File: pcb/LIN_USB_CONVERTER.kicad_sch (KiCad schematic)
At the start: 32 parts, among them J1 Conn_01x03, J2 TerminalBlock, J4 USB_C_Receptacle_USB2.0_16P, J6 Conn_ARM_SWD_TagConnect_TC203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, U1 TJA1028T/3V3/20/1J, U2 ISO7321CDR, U3 MCP1700T-3302ETT, U4 STM32F042G6U6

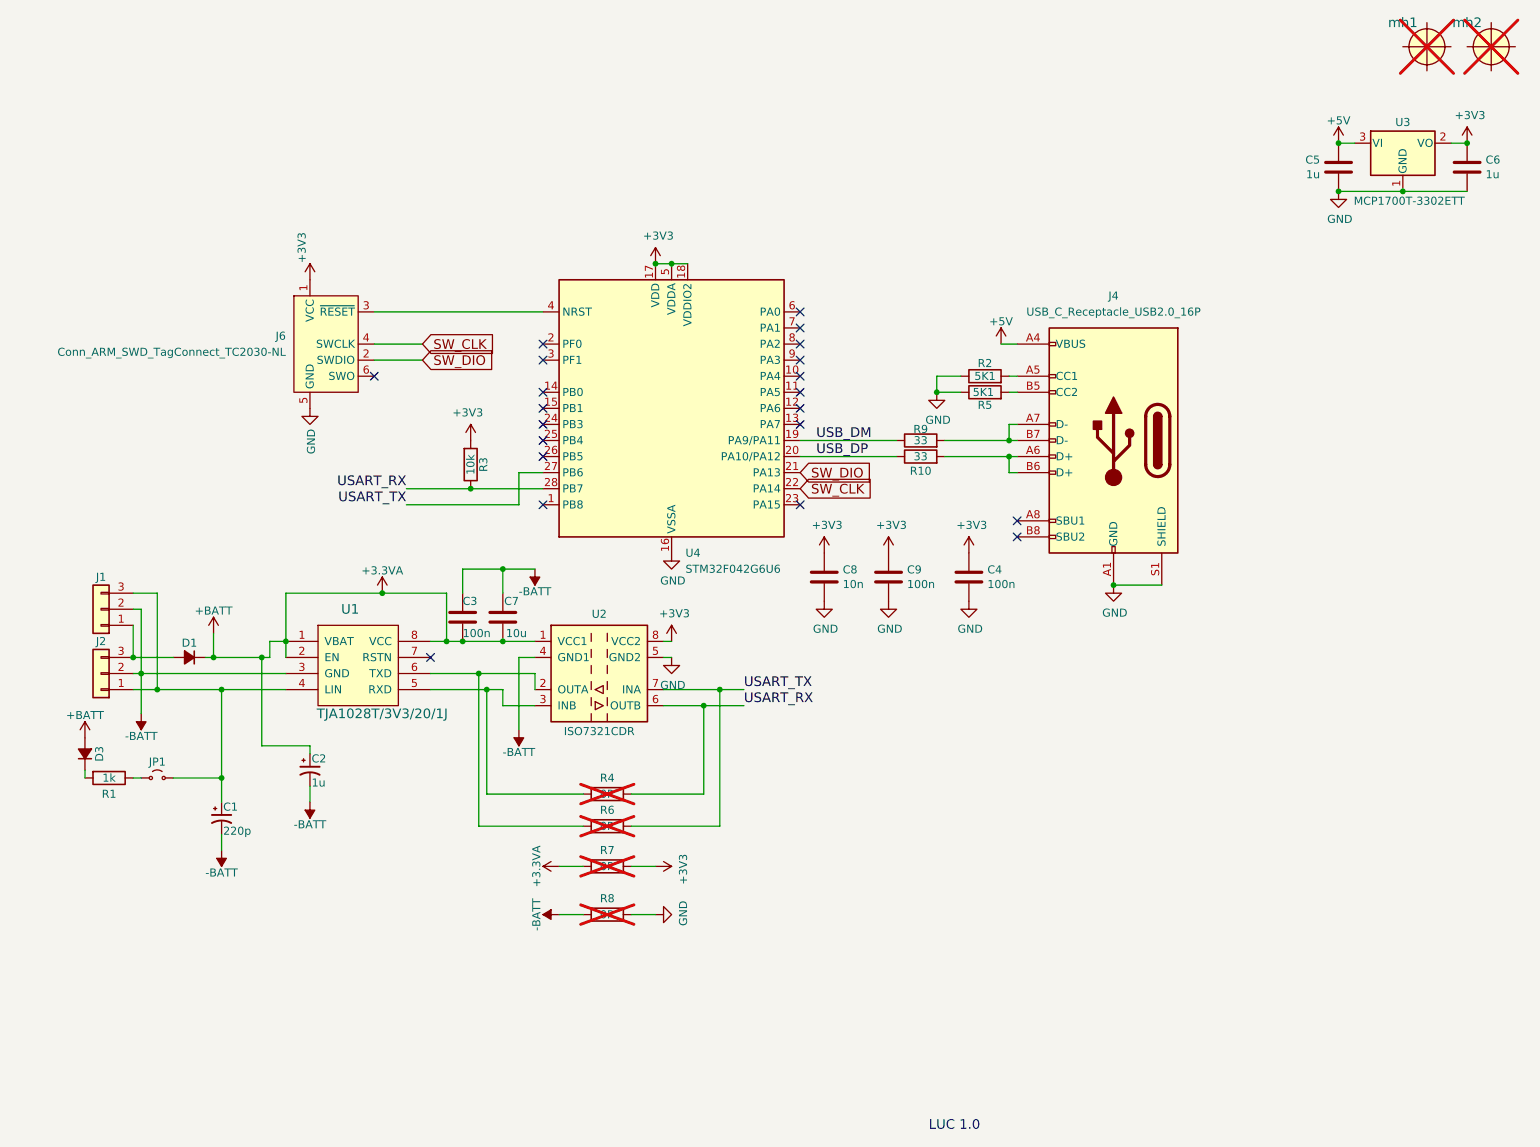
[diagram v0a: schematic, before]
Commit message: moved terminals to top, added mounting holes
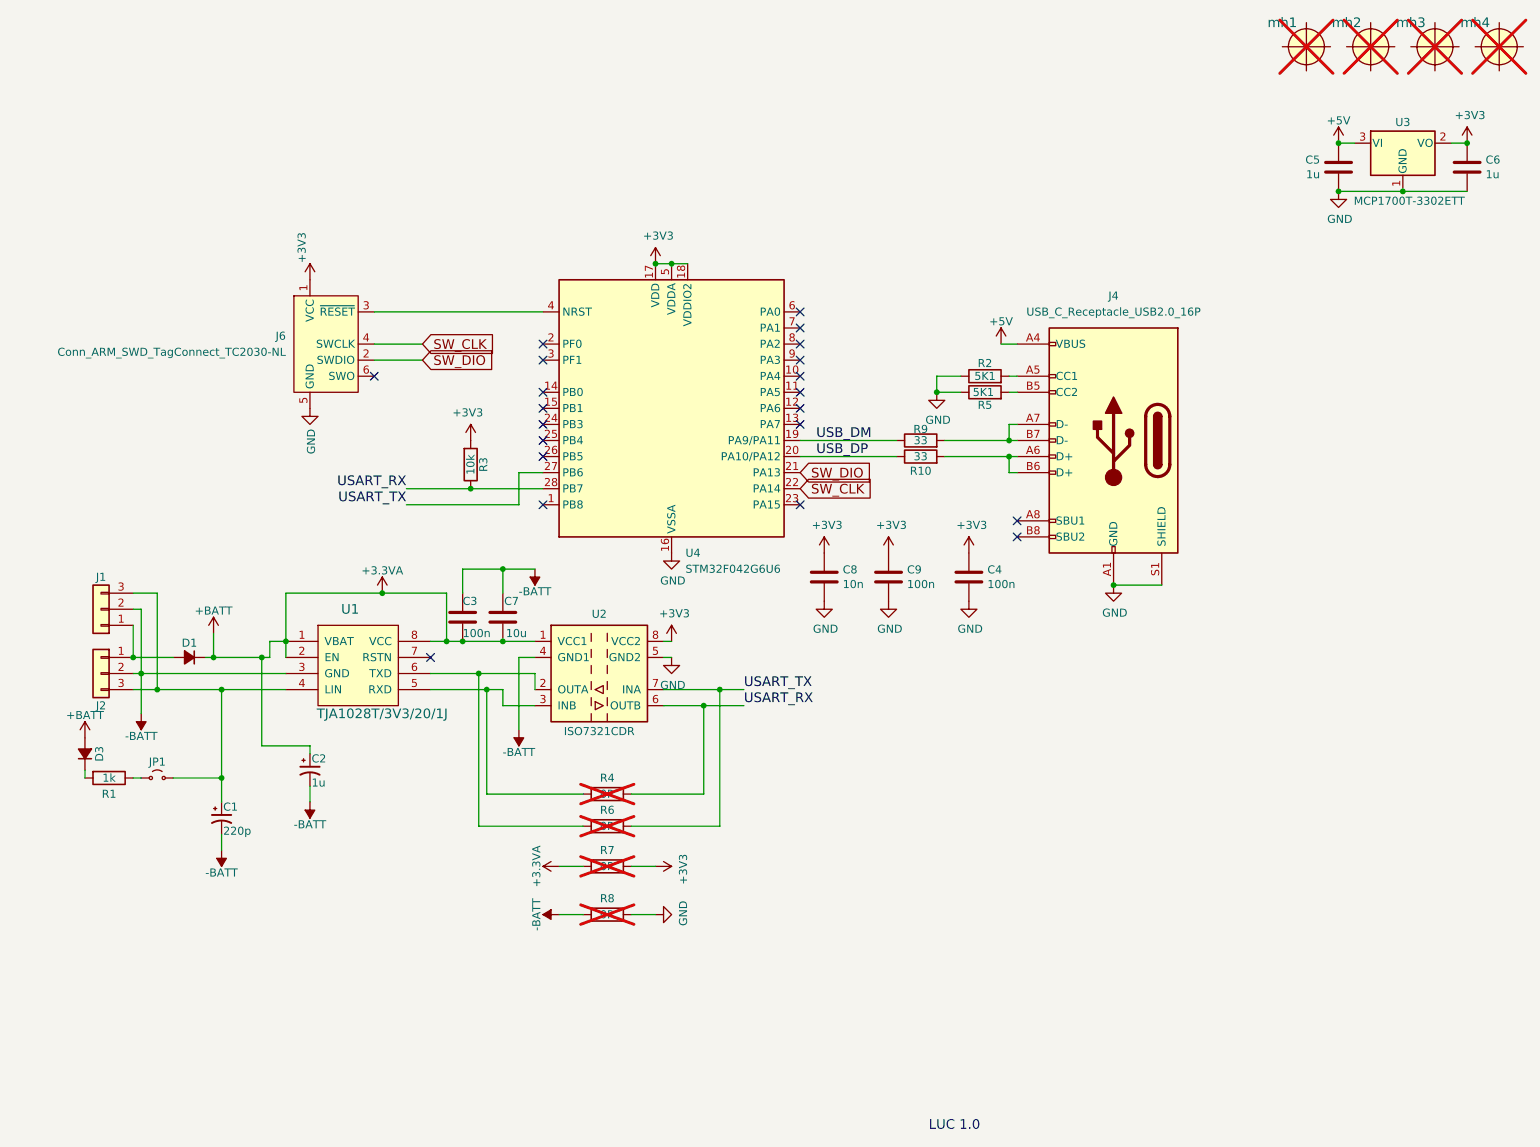
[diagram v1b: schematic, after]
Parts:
- added mh3, mh4: fiducial, usb_ccb_custom:1pin, symbol LIN_USB_CONVERTER-rescue:fiducial-RESCUE-LIN_USB_CONVERTER
- J1: LCSC Part # (none) -> C49257
- J2: footprint TerminalBlock:TerminalBlock_Altech_AK300-3_P5.00mm -> TerminalBlock_Phoenix:TerminalBlock_Phoenix_MKDS-1,5-3_1x03_P5.00mm_Horizontal; LCSC Part # (none) -> C424695; LSCS Part # C5188437 -> (none)
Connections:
- net at C1.1, J1.3 (Pin_3), JP1.2 (B)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: now also J2.3 (Pin_3); no longer J2.1 (Pin_1)
- net at D1.1 (A), J1.1 (Pin_1): now also J2.1 (Pin_1); no longer J2.3 (Pin_3)
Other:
- moved on the sheet: J2, mh1, mh2
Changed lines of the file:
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@@
 	(symbol
 		(lib_id "LIN_USB_CONVERTER-rescue:fiducial-RESCUE-LIN_USB_CONVERTER")
-		(at 266.7 19.05 0)
+		(at 247.65 19.05 0)
 		(unit 1)
 		(exclude_from_sim no)
@@
 		(dnp yes)
 		(property "Reference" "mh1"
-			(at 262.89 15.24 0)
+			(at 243.84 15.24 0)
 			(effects
 				(font
@@
 		)
 		(property "Value" "fiducial"
-			(at 273.05 25.4 0)
+			(at 254 25.4 0)
 			(effects
 				(font
@@
 		)
 		(property "Footprint" "usb_ccb_custom:1pin"
-			(at 266.7 19.05 0)
+			(at 247.65 19.05 0)
 			(effects
 				(font
@@
 		)
 		(property "Datasheet" ""
-			(at 266.7 19.05 0)
+			(at 247.65 19.05 0)
 			(effects
 				(font
@@
 		)
 		(property "Description" ""
-			(at 266.7 19.05 0)
+			(at 247.65 19.05 0)
 			(effects
 				(font
@@
 	(symbol
 		(lib_id "LIN_USB_CONVERTER-rescue:Conn_01x03-RESCUE-LIN_USB_CONVERTER")
-		(at 57.15 118.11 180)
+		(at 57.15 118.11 0)
+		(mirror y)
 		(unit 1)
 		(exclude_from_sim no)
@@
 		(dnp no)
 		(property "Reference" "J2"
-			(at 57.15 113.03 0)
+			(at 57.15 123.19 0)
 			(effects
 				(font
@@
 		)
 		(property "Value" "TerminalBlock"
-			(at 57.15 113.03 0)
+			(at 57.15 123.19 0)
 			(effects
 				(font
@@
 			)
 		)
-		(property "Footprint" "TerminalBlock:TerminalBlock_Altech_AK300-3_P5.00mm"
+		(property "Footprint" "TerminalBlock_Phoenix:TerminalBlock_Phoenix_MKDS-1,5-3_1x03_P5.00mm_Horizontal"
 			(at 57.15 118.11 0)
 			(effects
@@
 			)
 		)
-		(property "LSCS Part #" "C5188437"
+		(property "LCSC Part #" "C424695"
 			(at 57.15 118.11 0)
 			(effects
@@
 			)
 		)
+		(property "LCSC Part #" "C49257"
+			(at 57.15 107.95 0)
+			(effects
+				(font
+					(size 1.27 1.27)
+				)
+				(hide yes)
+			)
+		)
 		(pin "2"
 		)
@@
 	(symbol
 		(lib_id "LIN_USB_CONVERTER-rescue:fiducial-RESCUE-LIN_USB_CONVERTER")
-		(at 276.86 19.05 0)
+		(at 257.81 19.05 0)
 		(unit 1)
 		(exclude_from_sim no)
@@
 		(dnp yes)
 		(property "Reference" "mh2"
-			(at 273.05 15.24 0)
+			(at 254 15.24 0)
 			(effects
 				(font
@@
 		)
 		(property "Value" "fiducial"
-			(at 283.21 25.4 0)
+			(at 264.16 25.4 0)
 			(effects
 				(font
@@
 		)
 		(property "Footprint" "usb_ccb_custom:1pin"
-			(at 276.86 19.05 0)
+			(at 257.81 19.05 0)
 			(effects
 				(font
@@
 		)
 		(property "Datasheet" ""
-			(at 276.86 19.05 0)
+			(at 257.81 19.05 0)
 			(effects
 				(font
@@
 		)
 		(property "Description" ""
-			(at 276.86 19.05 0)
+			(at 257.81 19.05 0)
 			(effects
 				(font
@@
 					(unit 1)
 				)
+			)
+		)
+	)
+	(symbol
+		(lib_id "LIN_USB_CONVERTER-rescue:fiducial-RESCUE-LIN_USB_CONVERTER")
+		(at 267.97 19.05 0)
+		(unit 1)
+		(exclude_from_sim no)
+		(in_bom no)
+		(on_board yes)
+		(dnp yes)
+		(property "Reference" "mh3"
+			(at 264.16 15.24 0)
+			(effects
+				(font
+					(size 1.524 1.524)
+				)
+			)
+		)
+		(property "Value" "fiducial"
+			(at 274.32 25.4 0)
+			(effects
+				(font
+					(size 1.524 1.524)
+				)
+				(hide yes)
+			)
+		)
+		(property "Footprint" "usb_ccb_custom:1pin"
+			(at 267.97 19.05 0)
+			(effects
+				(font
+					(size 1.524 1.524)
+				)
+				(hide yes)
+			)
+		)
+		(property "Datasheet" ""
+			(at 267.97 19.05 0)
+			(effects
+				(font
+					(size 1.524 1.524)
+				)
+				(hide yes)
+			)
+		)
+		(property "Description" ""
+			(at 267.97 19.05 0)
+			(effects
+				(font
+					(size 1.27 1.27)
+				)
+				(hide yes)
+			)
+		)
+		(instances
+			(project "LIN_USB_CONVERTER"
+				(path "/d3cbf460-a65f-43bb-9c31-9907e36faf8d"
+					(reference "mh3")
+					(unit 1)
+				)
+			)
+		)
+	)
+	(symbol
+		(lib_id "LIN_USB_CONVERTER-rescue:fiducial-RESCUE-LIN_USB_CONVERTER")
+		(at 278.13 19.05 0)
+		(unit 1)
+		(exclude_from_sim no)
+		(in_bom no)
+		(on_board yes)
+		(dnp yes)
+		(property "Reference" "mh4"
+			(at 274.32 15.24 0)
+			(effects
+				(font
+					(size 1.524 1.524)
+				)
+			)
+		)
+		(property "Value" "fiducial"
+			(at 284.48 25.4 0)
+			(effects
+				(font
+					(size 1.524 1.524)
+				)
+				(hide yes)
+			)
+		)
+		(property "Footprint" "usb_ccb_custom:1pin"
+			(at 278.13 19.05 0)
+			(effects
+				(font
+					(size 1.524 1.524)
+				)
+				(hide yes)
+			)
+		)
+		(property "Datasheet" ""
+			(at 278.13 19.05 0)
+			(effects
+				(font
+					(size 1.524 1.524)
+				)
+				(hide yes)
+			)
+		)
+		(property "Description" ""
+			(at 278.13 19.05 0)
+			(effects
+				(font
+					(size 1.27 1.27)
+				)
+				(hide yes)
+			)
+		)
+		(instances
+			(project "LIN_USB_CONVERTER"
+				(path "/d3cbf460-a65f-43bb-9c31-9907e36faf8d"
+					(reference "mh4")
+					(unit 1)
+				)
